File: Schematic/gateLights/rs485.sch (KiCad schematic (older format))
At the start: 4 parts, among them U8 SP3485CN

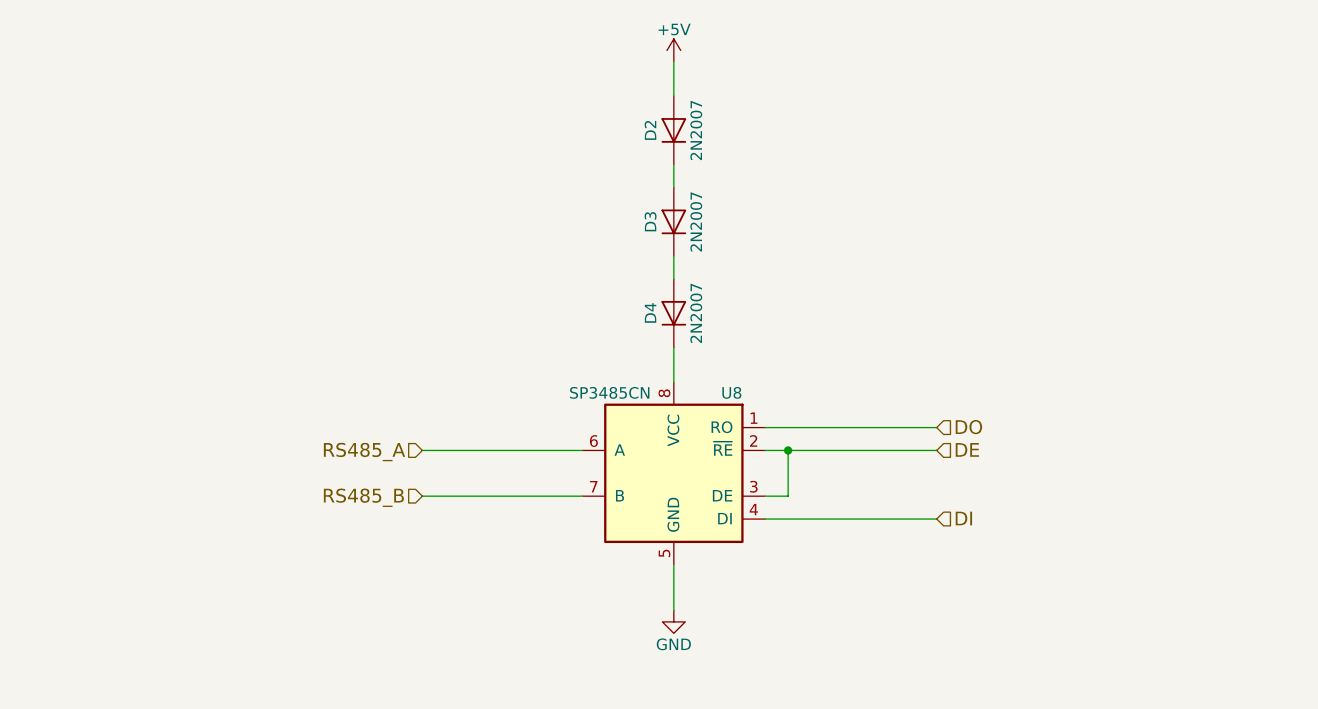
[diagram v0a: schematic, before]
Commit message: RS485 protection
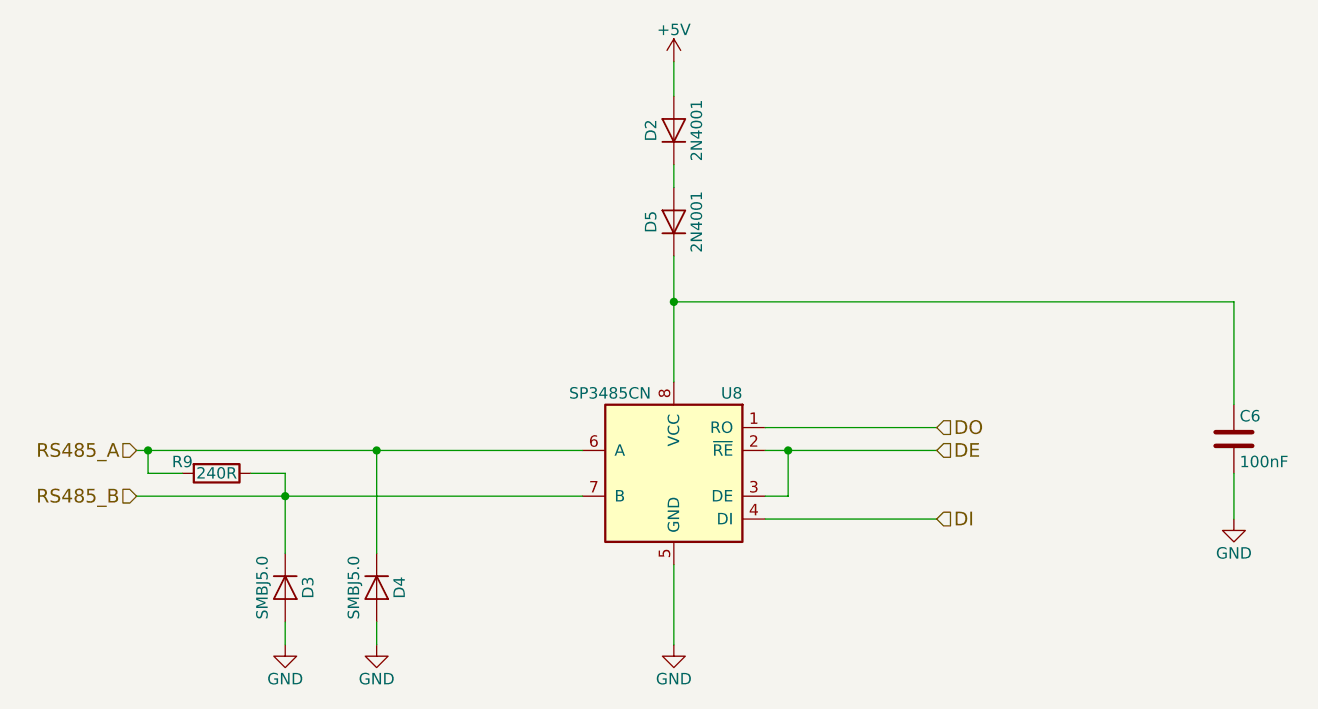
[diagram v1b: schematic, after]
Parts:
- added C6: 100nF, Capacitors_SMD:C_0603_HandSoldering, symbol C
- added D5: 2N4001, Diodes_THT:D_DO-15_P12.70mm_Horizontal, symbol D
- added R9: 240R, Resistors_SMD:R_1210_HandSoldering, symbol R
- D2: value 2N2007 -> 2N4001
- D3, D4: value 2N2007 -> SMBJ5.0; footprint Diodes_THT:D_DO-15_P12.70mm_Horizontal -> Diodes_SMD:D_SMB_Handsoldering
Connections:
- net GND: now also D3.2 (A), D4.2 (A), C6.2
- net RS485_A: now also D4.1 (K), R9.2
- net RS485_B: now also D3.1 (K), R9.1
- net at U8.8 (VCC): now also C6.1, D5.1 (K); no longer D4.1 (K)
- net at D2.1 (K): now also D5.2 (A); no longer D3.2 (A)
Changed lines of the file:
@@
 	-1   0    0    -1
 $EndComp
-Text HLabel 3700 3800 0    60   Input ~ 0
+Text HLabel 2450 3800 0    60   Input ~ 0
 RS485_A
-Text HLabel 3700 4000 0    60   Input ~ 0
+Text HLabel 2450 4000 0    60   Input ~ 0
 RS485_B
 Text HLabel 5950 3800 2    60   Input ~ 0
@@
 	5950 3700 5200 3700
 Wire Wire Line
-	4400 3800 3700 3800
+	4400 3800 2450 3800
 Wire Wire Line
-	4400 4000 3700 4000
+	4400 4000 2450 4000
 $Comp
-L GND #PWR017
+L GND #PWR21
 U 1 1 59208970
-P 4800 4500
-F 0 "#PWR017" H 4800 4250 50  0001 C CNN
-F 1 "GND" H 4800 4350 50  0000 C CNN
-F 2 "" H 4800 4500 50  0001 C CNN
-F 3 "" H 4800 4500 50  0001 C CNN
-	1    4800 4500
+P 4800 4650
+F 0 "#PWR21" H 4800 4400 50  0001 C CNN
+F 1 "GND" H 4800 4500 50  0000 C CNN
+F 2 "" H 4800 4650 50  0001 C CNN
+F 3 "" H 4800 4650 50  0001 C CNN
+	1    4800 4650
 	1    0    0    -1
 $EndComp
 Wire Wire Line
-	4800 4500 4800 4300
+	4800 4650 4800 4300
 $Comp
 L D D2
@@
 P 4800 2400
 F 0 "D2" H 4800 2500 50  0000 C CNN
-F 1 "2N2007" H 4800 2300 50  0000 C CNN
+F 1 "2N4001" H 4800 2300 50  0000 C CNN
 F 2 "Diodes_THT:D_DO-15_P12.70mm_Horizontal" H 4800 2400 50  0001 C CNN
-F 3 "" H 4800 2400 50  0001 C CNN
+F 3 "http://docs-europe.electrocomponents.com/webdocs/137d/0900766b8137d734.pdf" H 4800 2400 50  0001 C CNN
 	1    4800 2400
 	0    -1   -1   0
 $EndComp
 $Comp
-L +5V #PWR018
+L +5V #PWR20
 U 1 1 59208A37
 P 4800 2100
-F 0 "#PWR018" H 4800 1950 50  0001 C CNN
+F 0 "#PWR20" H 4800 1950 50  0001 C CNN
 F 1 "+5V" H 4800 2240 50  0000 C CNN
 F 2 "" H 4800 2100 50  0001 C CNN
@@
 	4800 2550 4800 2650
 Wire Wire Line
-	4800 2950 4800 3050
-Wire Wire Line
-	4800 3350 4800 3500
+	4800 2950 4800 3500
 $Comp
-L D D3
-U 1 1 59208AB8
+L D D5
+U 1 1 5922AA27
 P 4800 2800
-F 0 "D3" H 4800 2900 50  0000 C CNN
-F 1 "2N2007" H 4800 2700 50  0000 C CNN
+F 0 "D5" H 4800 2900 50  0000 C CNN
+F 1 "2N4001" H 4800 2700 50  0000 C CNN
 F 2 "Diodes_THT:D_DO-15_P12.70mm_Horizontal" H 4800 2800 50  0001 C CNN
-F 3 "" H 4800 2800 50  0001 C CNN
+F 3 "http://docs-europe.electrocomponents.com/webdocs/137d/0900766b8137d734.pdf" H 4800 2800 50  0001 C CNN
 	1    4800 2800
 	0    -1   -1   0
 $EndComp
 $Comp
+L D D3
+U 1 1 5923CAE9
+P 3100 4400
+F 0 "D3" H 3100 4500 50  0000 C CNN
+F 1 "SMBJ5.0" H 3100 4300 50  0000 C CNN
+F 2 "Diodes_SMD:D_SMB_Handsoldering" H 3100 4400 50  0001 C CNN
+F 3 "http://docs-europe.electrocomponents.com/webdocs/137d/0900766b8137d734.pdf" H 3100 4400 50  0001 C CNN
+	1    3100 4400
+	0    1    1    0
+$EndComp
+$Comp
 L D D4
-U 1 1 59208ADD
-P 4800 3200
-F 0 "D4" H 4800 3300 50  0000 C CNN
-F 1 "2N2007" H 4800 3100 50  0000 C CNN
-F 2 "Diodes_THT:D_DO-15_P12.70mm_Horizontal" H 4800 3200 50  0001 C CNN
-F 3 "" H 4800 3200 50  0001 C CNN
-	1    4800 3200
-	0    -1   -1   0
+U 1 1 5923CB61
+P 3500 4400
+F 0 "D4" H 3500 4500 50  0000 C CNN
+F 1 "SMBJ5.0" H 3500 4300 50  0000 C CNN
+F 2 "Diodes_SMD:D_SMB_Handsoldering" H 3500 4400 50  0001 C CNN
+F 3 "http://docs-europe.electrocomponents.com/webdocs/137d/0900766b8137d734.pdf" H 3500 4400 50  0001 C CNN
+	1    3500 4400
+	0    1    1    0
 $EndComp
+$Comp
+L GND #PWR19
+U 1 1 5923CB97
+P 3500 4650
+F 0 "#PWR19" H 3500 4400 50  0001 C CNN
+F 1 "GND" H 3500 4500 50  0000 C CNN
+F 2 "" H 3500 4650 50  0001 C CNN
+F 3 "" H 3500 4650 50  0001 C CNN
+	1    3500 4650
+	1    0    0    -1
+$EndComp
+$Comp
+L GND #PWR18
+U 1 1 5923CBC5
+P 3100 4650
+F 0 "#PWR18" H 3100 4400 50  0001 C CNN
+F 1 "GND" H 3100 4500 50  0000 C CNN
+F 2 "" H 3100 4650 50  0001 C CNN
+F 3 "" H 3100 4650 50  0001 C CNN
+	1    3100 4650
+	1    0    0    -1
+$EndComp
+Wire Wire Line
+	3100 4550 3100 4650
+Wire Wire Line
+	3500 4550 3500 4650
+Wire Wire Line
+	3500 4250 3500 3800
+Connection ~ 3500 3800
+Wire Wire Line
+	3100 3900 3100 4250
+Connection ~ 3100 4000
+$Comp
+L R R9
+U 1 1 5923CC32
+P 2800 3900
+F 0 "R9" V 2750 3750 50  0000 C CNN
+F 1 "240R" V 2800 3900 50  0000 C CNN
+F 2 "Resistors_SMD:R_1210_HandSoldering" V 2730 3900 50  0001 C CNN
+F 3 "" H 2800 3900 50  0001 C CNN
+	1    2800 3900
+	0    1    1    0
+$EndComp
+Wire Wire Line
+	2950 3900 3100 3900
+Wire Wire Line
+	2650 3900 2500 3900
+Wire Wire Line
+	2500 3900 2500 3800
+Connection ~ 2500 3800
+$Comp
+L C C6
+U 1 1 592480DF
+P 7250 3750
+F 0 "C6" H 7275 3850 50  0000 L CNN
+F 1 "100nF" H 7275 3650 50  0000 L CNN
+F 2 "Capacitors_SMD:C_0603_HandSoldering" H 7288 3600 50  0001 C CNN
+F 3 "" H 7250 3750 50  0001 C CNN
+	1    7250 3750
+	1    0    0    -1
+$EndComp
+$Comp
+L GND #PWR22
+U 1 1 592480E6
+P 7250 4100
+F 0 "#PWR22" H 7250 3850 50  0001 C CNN
+F 1 "GND" H 7250 3950 50  0000 C CNN
+F 2 "" H 7250 4100 50  0001 C CNN
+F 3 "" H 7250 4100 50  0001 C CNN
+	1    7250 4100
+	1    0    0    -1
+$EndComp
+Wire Wire Line
+	7250 3150 7250 3600
+Wire Wire Line
+	7250 3900 7250 4100
+Wire Wire Line
+	7250 3150 4800 3150
+Connection ~ 4800 3150
 $EndSCHEMATC

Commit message: Fix resistor footprints
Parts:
- R9: footprint Resistors_SMD:R_1210_HandSoldering -> Resistors_SMD:R_1206_HandSoldering
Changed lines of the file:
@@
 F 0 "R9" V 2750 3750 50  0000 C CNN
 F 1 "240R" V 2800 3900 50  0000 C CNN
-F 2 "Resistors_SMD:R_1210_HandSoldering" V 2730 3900 50  0001 C CNN
+F 2 "Resistors_SMD:R_1206_HandSoldering" V 2730 3900 50  0001 C CNN
 F 3 "" H 2800 3900 50  0001 C CNN
 	1    2800 3900
